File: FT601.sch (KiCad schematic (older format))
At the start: 23 parts, among them U1 FT601, U2 ESD7016, U4 ECP5, U5 Si5351, X1 GSB443133HR, Y1 FL3000027, Y2 ABM11-141-26.000MHZ

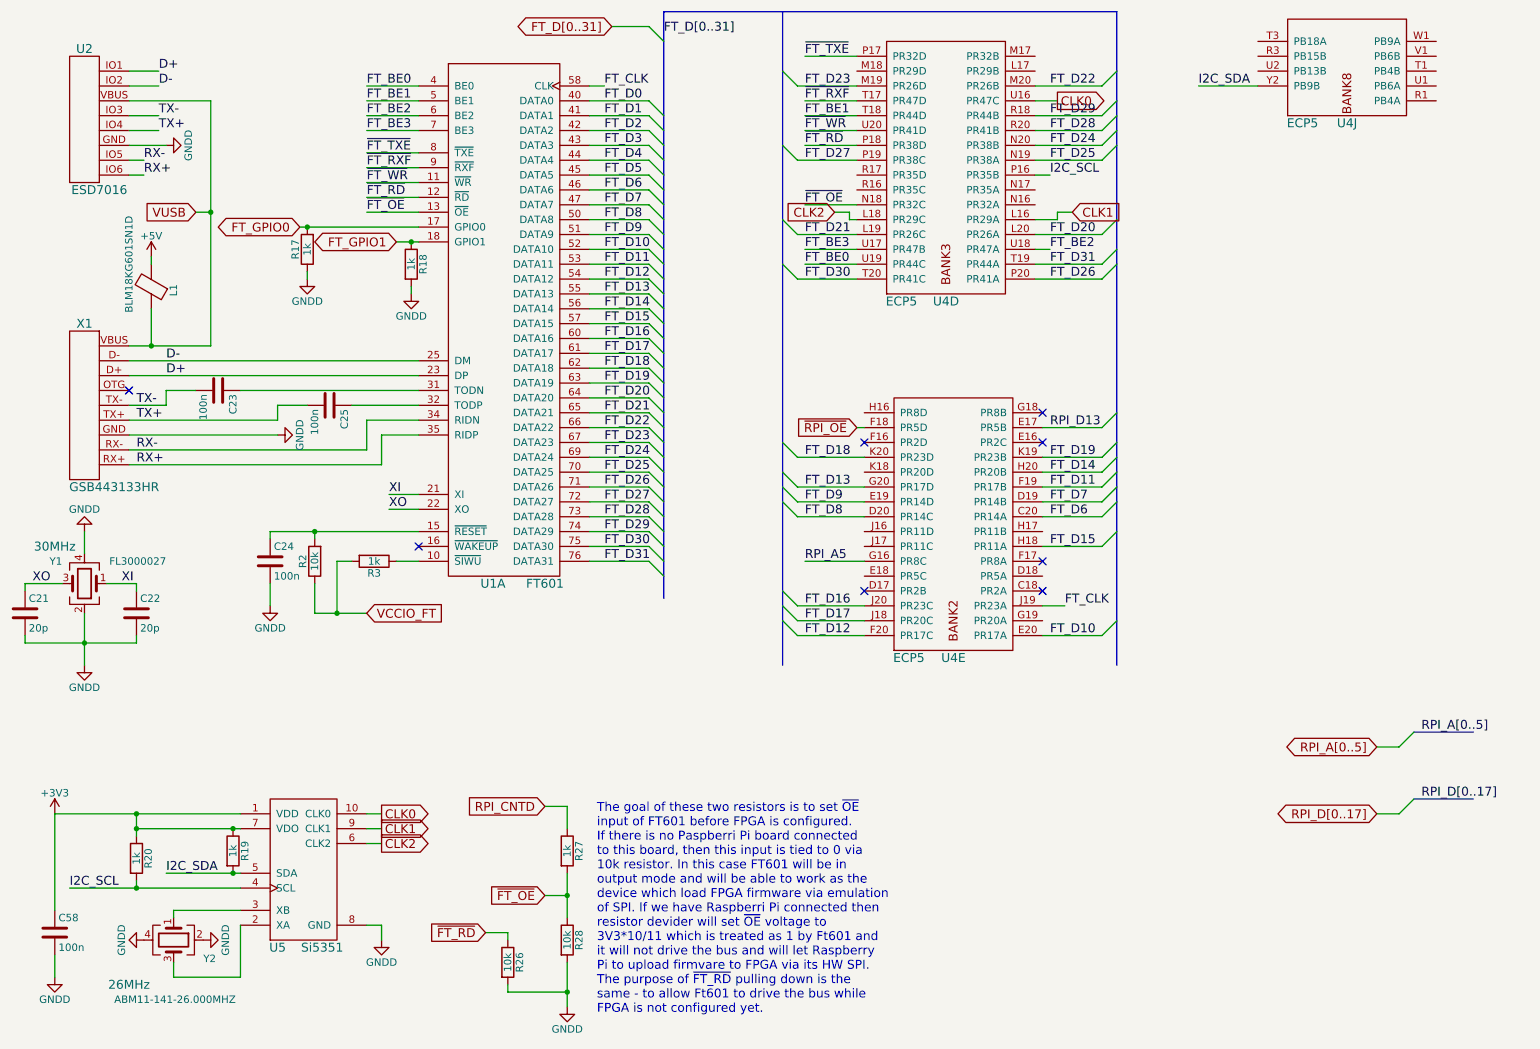
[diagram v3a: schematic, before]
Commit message: Changed RF sheet to add second path to TX and RX
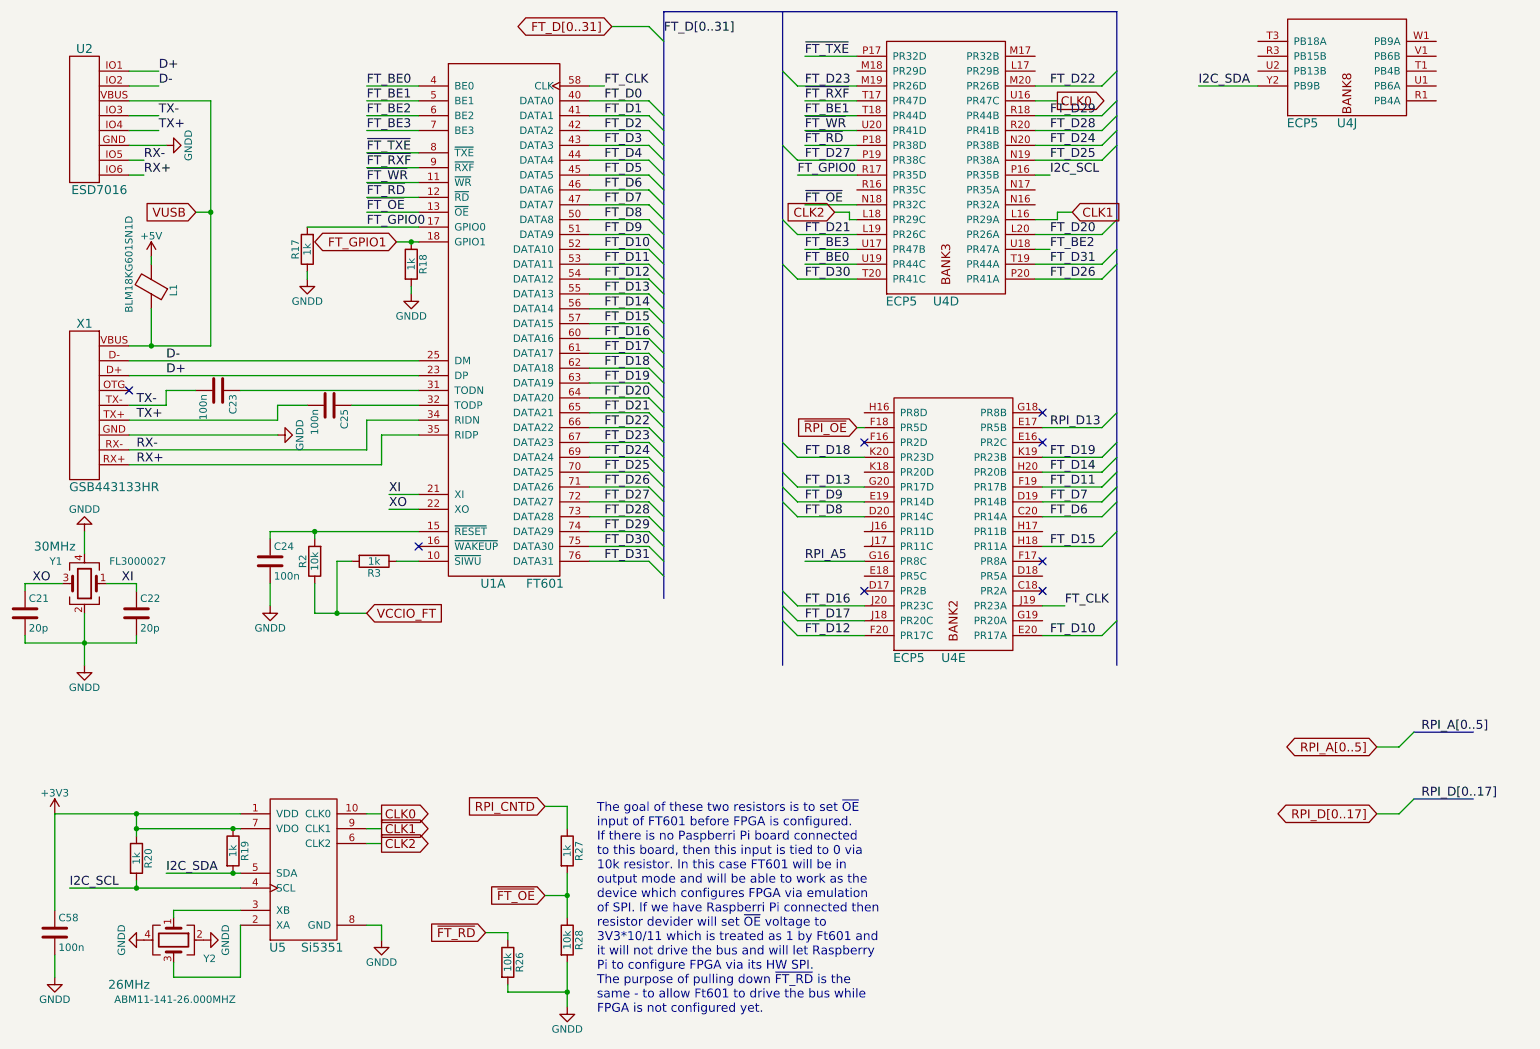
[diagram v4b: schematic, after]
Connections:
- net FT_GPIO0: now also U4.R17 (PR35D)
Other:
- note added: "The goal of these two resistors is to set ~OE~\ninput of FT601 before FPGA is configured.\nIf there is no Paspberri Pi board connected\nto this board, then this input is tied to 0 via\n10k resistor. In this case FT601 will be in\noutput mode and will be able to work as the\ndevice which configures FPGA via emulation\nof SPI. If we have Raspberri Pi connected then \nresistor devider will set ~OE~ 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"
- note removed: "The goal of these two resistors is to set ~OE~\ninput of FT601 before FPGA is configured.\nIf there is no Paspberri Pi board connected\nto this board, then this input is tied to 0 via\n10k resistor. In this case FT601 will be in\noutput mode and will be able to work as the\ndevice which load FPGA firmware via emulation\nof SPI. If we have Raspberri Pi connected then \nresistor devider will set ~O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"
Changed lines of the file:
@@
 $EndComp
 $Comp
-L GNDD #PWR053
+L GNDD #PWR68
 U 1 1 58981141
 P 2550 3650
-F 0 "#PWR053" H 2550 3400 50  0001 C CNN
+F 0 "#PWR68" H 2550 3400 50  0001 C CNN
 F 1 "GNDD" H 2550 3500 50  0000 C CNN
 F 2 "" H 2550 3650 50  0000 C CNN
@@
 TX+
 $Comp
-L GNDD #PWR054
+L GNDD #PWR65
 U 1 1 58982448
 P 1800 1700
-F 0 "#PWR054" H 1800 1450 50  0001 C CNN
+F 0 "#PWR65" H 1800 1450 50  0001 C CNN
 F 1 "GNDD" H 1800 1550 50  0000 C CNN
 F 2 "" H 1800 1700 50  0000 C CNN
@@
 $EndComp
 $Comp
-L GNDD #PWR055
+L GNDD #PWR67
 U 1 1 58983172
 P 2500 4800
-F 0 "#PWR055" H 2500 4550 50  0001 C CNN
+F 0 "#PWR67" H 2500 4550 50  0001 C CNN
 F 1 "GNDD" H 2500 4650 50  0000 C CNN
 F 2 "" H 2500 4800 50  0000 C CNN
@@
 $EndComp
 $Comp
-L GNDD #PWR056
+L GNDD #PWR62
 U 1 1 58983AFE
 P 1250 5200
-F 0 "#PWR056" H 1250 4950 50  0001 C CNN
+F 0 "#PWR62" H 1250 4950 50  0001 C CNN
 F 1 "GNDD" H 1250 5050 50  0000 C CNN
 F 2 "" H 1250 5200 50  0000 C CNN
@@
 $EndComp
 $Comp
-L GNDD #PWR057
+L GNDD #PWR61
 U 1 1 58983B6B
 P 1250 4300
-F 0 "#PWR057" H 1250 4050 50  0001 C CNN
+F 0 "#PWR61" H 1250 4050 50  0001 C CNN
 F 1 "GNDD" H 1250 4150 50  0000 C CNN
 F 2 "" H 1250 4300 50  0000 C CNN
@@
 $EndComp
 $Comp
-L GNDD #PWR058
+L GNDD #PWR71
 U 1 1 58A3CED9
 P 3450 2700
-F 0 "#PWR058" H 3450 2450 50  0001 C CNN
+F 0 "#PWR71" H 3450 2450 50  0001 C CNN
 F 1 "GNDD" H 3450 2550 50  0000 C CNN
 F 2 "" H 3450 2700 50  0000 C CNN
@@
 $EndComp
 $Comp
-L GNDD #PWR059
+L GNDD #PWR69
 U 1 1 58A3CF07
 P 2750 2600
-F 0 "#PWR059" H 2750 2350 50  0001 C CNN
+F 0 "#PWR69" H 2750 2350 50  0001 C CNN
 F 1 "GNDD" H 2750 2450 50  0000 C CNN
 F 2 "" H 2750 2600 50  0000 C CNN
@@
 $EndComp
 $Comp
-L +3V3 #PWR060
+L +3V3 #PWR59
 U 1 1 58A3E1D8
 P 1050 6200
-F 0 "#PWR060" H 1050 6050 50  0001 C CNN
+F 0 "#PWR59" H 1050 6050 50  0001 C CNN
 F 1 "+3V3" H 1050 6340 50  0000 C CNN
 F 2 "" H 1050 6200 50  0000 C CNN
@@
 $EndComp
 $Comp
-L GNDD #PWR061
+L GNDD #PWR60
 U 1 1 58A3E3AE
 P 1050 7300
-F 0 "#PWR061" H 1050 7050 50  0001 C CNN
+F 0 "#PWR60" H 1050 7050 50  0001 C CNN
 F 1 "GNDD" H 1050 7150 50  0000 C CNN
 F 2 "" H 1050 7300 50  0000 C CNN
@@
 $EndComp
 $Comp
-L GNDD #PWR062
+L GNDD #PWR66
 U 1 1 58A3F555
 P 2050 7050
-F 0 "#PWR062" H 2050 6800 50  0001 C CNN
+F 0 "#PWR66" H 2050 6800 50  0001 C CNN
 F 1 "GNDD" H 2050 6900 50  0000 C CNN
 F 2 "" H 2050 7050 50  0000 C CNN
@@
 CLK2
 $Comp
-L GNDD #PWR063
+L GNDD #PWR70
 U 1 1 58A415AA
 P 3250 7050
-F 0 "#PWR063" H 3250 6800 50  0001 C CNN
+F 0 "#PWR70" H 3250 6800 50  0001 C CNN
 F 1 "GNDD" H 3250 6900 50  0000 C CNN
 F 2 "" H 3250 7050 50  0000 C CNN
@@
 $EndComp
 $Comp
-L +5V #PWR064
+L +5V #PWR64
 U 1 1 58A3FC7D
 P 1700 2450
-F 0 "#PWR064" H 1700 2300 50  0001 C CNN
+F 0 "#PWR64" H 1700 2300 50  0001 C CNN
 F 1 "+5V" H 1700 2590 50  0000 C CNN
 F 2 "" H 1700 2450 50  0000 C CNN
@@
 Connection ~ 3450 2350
 Wire Wire Line
-	2700 2250 3500 2250
-Connection ~ 2750 2250
-Wire Wire Line
 	2750 2600 2750 2550
 Wire Wire Line
@@
 	1050 6200 1050 6850
 $Comp
-L GNDD #PWR065
+L GNDD #PWR63
 U 1 1 58A3F51F
 P 1650 7050
-F 0 "#PWR065" H 1650 6800 50  0001 C CNN
+F 0 "#PWR63" H 1650 6800 50  0001 C CNN
 F 1 "GNDD" H 1650 6900 50  0000 C CNN
 F 2 "" H 1650 7050 50  0000 C CNN
@@
 Text GLabel 4800 900  0    60   BiDi ~ 0
 FT_D[0..31]
-Text GLabel 2700 2250 0    60   BiDi ~ 0
-FT_GPIO0
 Text GLabel 3350 2350 0    60   BiDi ~ 0
 FT_GPIO1
@@
 ~FT_OE
 $Comp
-L GNDD #PWR066
+L GNDD #PWR72
 U 1 1 58ABB46B
 P 4500 7500
-F 0 "#PWR066" H 4500 7250 50  0001 C CNN
+F 0 "#PWR72" H 4500 7250 50  0001 C CNN
 F 1 "GNDD" H 4500 7350 50  0000 C CNN
 F 2 "" H 4500 7500 50  0000 C CNN
@@
 Connection ~ 4500 6750
 Text Notes 4700 7550 0    60   ~ 0
-The goal of these two resistors is to set ~OE~\ninput of FT601 before FPGA is configured.\nIf there is no Paspberri Pi board connected\nto this board, then this input is tied to 0 via\n10k resistor. In this case FT601 will be in\noutput mode and will be able to work as the\ndevice which load FPGA firmware via emulation\nof SPI. If we have Raspberri Pi connected then \nresistor devider will set ~OE~ voltage to\n3V3*10/11 which is treated as 1 by Ft601 and\nit will not drive the bus and will let Raspberry\nPi to upload firmvare to FPGA via its HW SPI.\nThe purpose of ~FT_RD~ pulling down is the \nsame - to allow Ft601 to drive the bus while \nFPGA is not configured yet.
+The goal of these two resistors is to set ~OE~\ninput of FT601 before FPGA is configured.\nIf there is no Paspberri Pi board connected\nto this board, then this input is tied to 0 via\n10k resistor. In this case FT601 will be in\noutput mode and will be able to work as the\ndevice which configures FPGA via emulation\nof SPI. If we have Raspberri Pi connected then \nresistor devider will set ~OE~ voltage to\n3V3*10/11 which is treated as 1 by Ft601 and\nit will not drive the bus and will let Raspberry\nPi to configure FPGA via its HW SPI.\nThe purpose of pulling down ~FT_RD~ is the \nsame - to allow Ft601 to drive the bus while \nFPGA is not configured yet.
 Text GLabel 3950 7000 0    60   Input ~ 0
 ~FT_RD
@@
 Wire Wire Line
 	6450 1400 6100 1400
+Text Label 3150 2250 0    60   ~ 0
+FT_GPIO0
+Wire Wire Line
+	2750 2250 3500 2250
+Text Label 6050 1900 0    60   ~ 0
+FT_GPIO0
+Wire Wire Line
+	6450 1900 6050 1900
 $EndSCHEMATC

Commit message: Add schematic of FT232H. Not placed yet.
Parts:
- L1: footprint Capacitors_SMD:C_0805 -> Inductors_SMD:L_0805
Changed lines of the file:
@@
 F 0 "L1" V 1550 2675 50  0000 C CNN
 F 1 "BLM18KG601SN1D" V 1850 2500 50  0000 C CNN
-F 2 "Capacitors_SMD:C_0805" V 1630 2650 50  0001 C CNN
+F 2 "Inductors_SMD:L_0805" V 1630 2650 50  0001 C CNN
 F 3 "" H 1700 2650 50  0000 C CNN
 	1    1700 2650
